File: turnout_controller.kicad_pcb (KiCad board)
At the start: 2 copper layers, 1 part

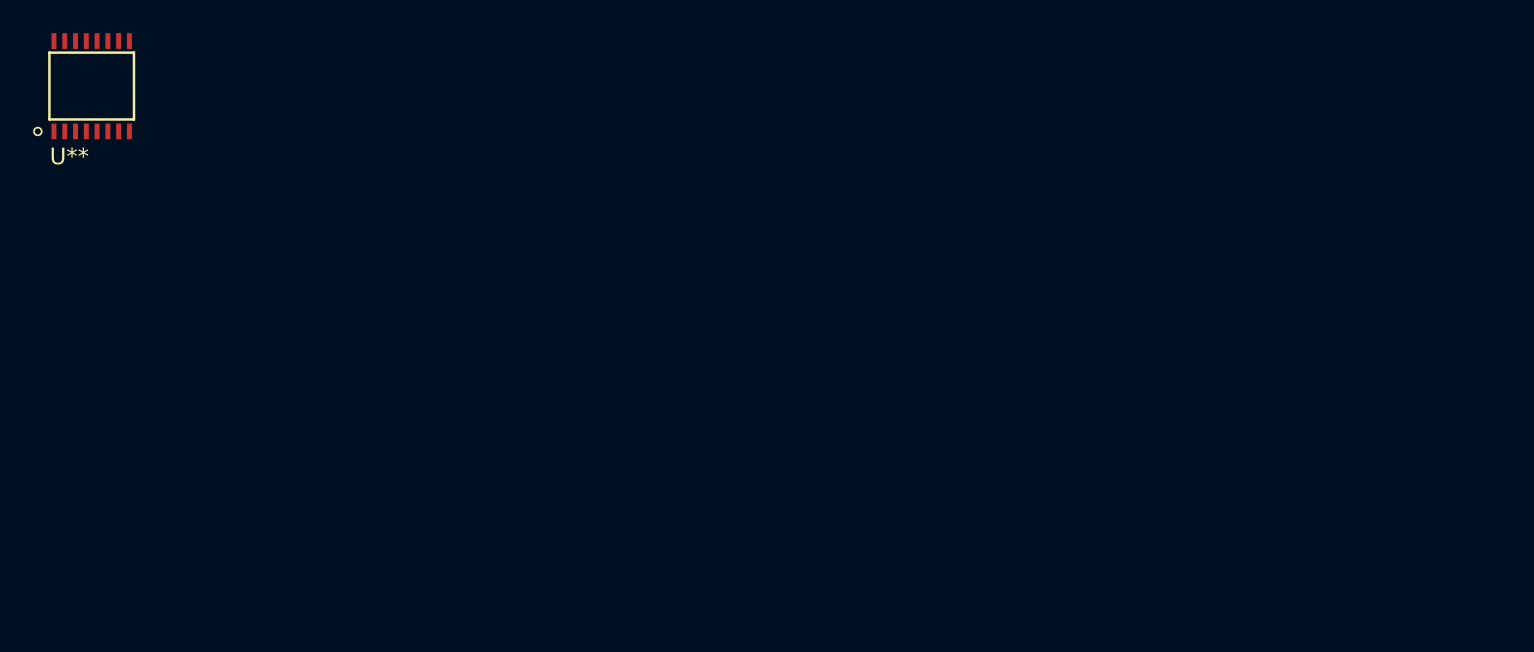
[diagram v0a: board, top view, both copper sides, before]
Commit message: Includes:
New project file
Footprints for buttons, bridge rectifier and edge connectors
initial circuit board layout
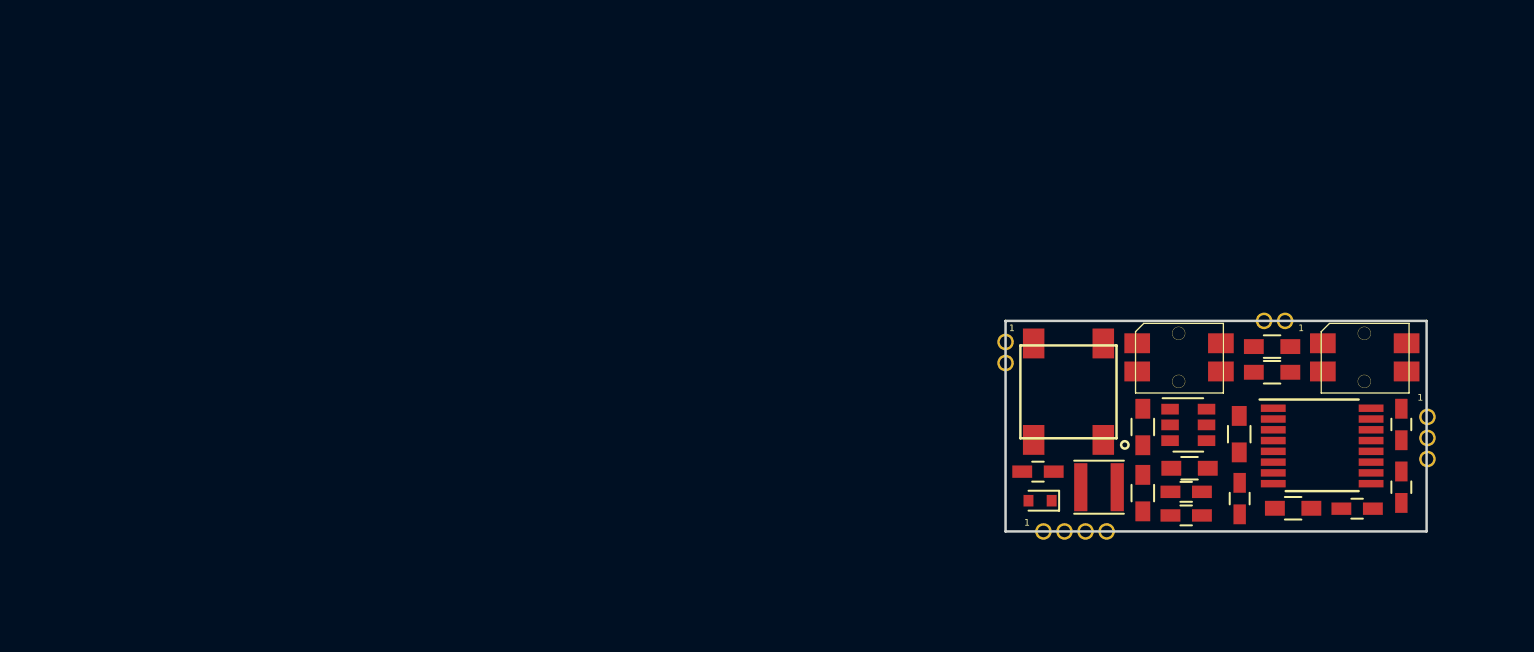
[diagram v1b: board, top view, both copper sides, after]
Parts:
- removed U**: MKE04-TSSOP16, mke04:MKE04-TSSOP16
- added C1: 22u, Capacitors_SMD:C_0603_HandSoldering, F.Cu at (149.6, 82.7)
- added C2: 1u, Capacitors_SMD:C_0603_HandSoldering, F.Cu at (149.6, 84.1)
- added C3: 22u, Capacitors_SMD:C_0603_HandSoldering, F.Cu at (140.6, 81.5)
- added C4: 22u, Capacitors_SMD:C_0603_HandSoldering, F.Cu at (152.8, 83.1)
- added C5: 1u, Capacitors_SMD:C_0603_HandSoldering, F.Cu at (159.9, 83.7)
- added C6: 0.1u, Capacitors_SMD:C_0603_HandSoldering, F.Cu at (162.6, 82.4)
- added C7: 22u, Capacitors_SMD:C_0603_HandSoldering, F.Cu at (162.6, 78.6)
- added D1: D_Schottky, Diodes_SMD:D_SOD-523, F.Cu at (140.8, 83.2)
- added D2: CZ4GP208-HF, Z4GP208-HF:Z4GP208-HF-SMD, F.Cu at (140.0, 75.9)
- added J1: DCC Input, half-connectors:Socket_Strip_Straight_1x02_Pitch1.27mm_at_edge, F.Cu at (138.7, 73.7)
- added J2: Conn_01x04, half-connectors:Socket_Strip_Straight_1x04_Pitch1.27mm_at_edge, F.Cu at (141.0, 85.1)
- added J3: Servo Motor, half-connectors:Socket_Strip_Straight_1x03_Pitch1.27mm_at_edge, F.Cu at (164.1, 78.2)
- added J4: LED Connect, half-connectors:Socket_Strip_Straight_1x02_Pitch1.27mm_at_edge, F.Cu at (155.5, 72.4)
- added L1: 4.7u, Inductors_SMD:L_Taiyo-Yuden_NR-30xx, F.Cu at (144.3, 82.4)
- added R1: 100K, Resistors_SMD:R_0603_HandSoldering, F.Cu at (149.8, 81.3)
- added R2: 10K, Resistors_SMD:R_0603_HandSoldering, F.Cu at (147.0, 82.8)
- added R3: 4.7K, Resistors_SMD:R_0603_HandSoldering, F.Cu at (147.0, 78.8)
- added R4: 59K, Resistors_SMD:R_0603_HandSoldering, F.Cu at (154.8, 75.5)
- added R5: 7.68K, Resistors_SMD:R_0603_HandSoldering, F.Cu at (156.0, 83.7)
- added R6: 40.2K, Resistors_SMD:R_0603_HandSoldering, F.Cu at (152.8, 79.2)
- added R7: 400, Resistors_SMD:R_0603_HandSoldering, F.Cu at (154.8, 73.9)
- added SW1: SW_Push, tt_buttons:HTB1-Button, F.Cu at (162.0, 72.3)
- added SW2: SW_Push, tt_buttons:HTB1-Button, F.Cu at (150.8, 72.3)
- added U1: AP65111A, TO_SOT_Packages_SMD:SOT-23-6, F.Cu at (149.7, 78.7)
- added U2: MKE04P24M48SF0, Housings_SSOP:TSSOP-16_4.4x5mm_Pitch0.65mm, F.Cu at (157.8, 79.9)
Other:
- board outline added: 25.4 x 12.7 mm
- board text added: "1"

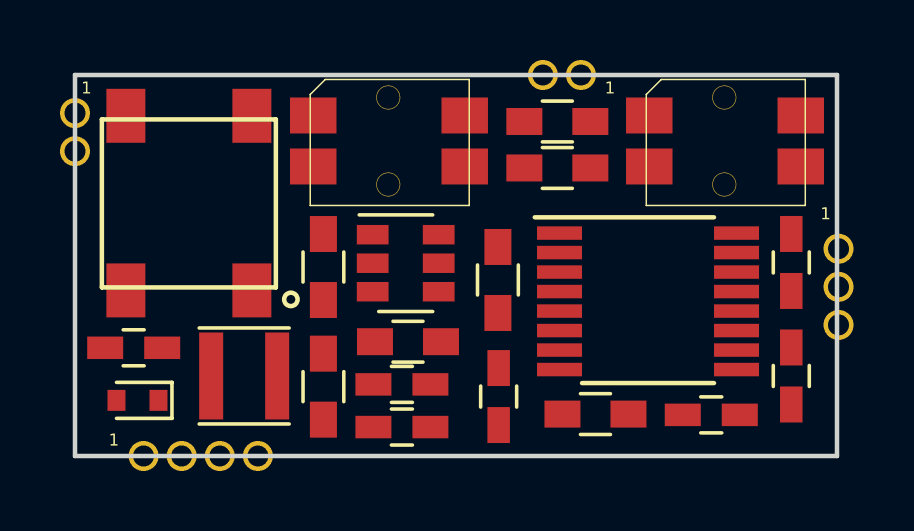
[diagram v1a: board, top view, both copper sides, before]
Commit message: 1. New PCB layout based around new positioning of buttons.
2. Optimizing distance between buck circuit components.

3. Added optional on-board LEDs.
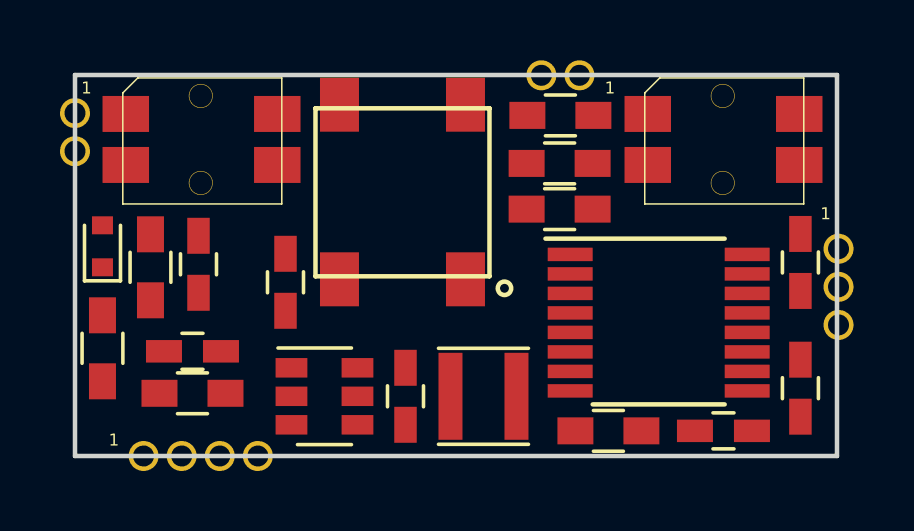
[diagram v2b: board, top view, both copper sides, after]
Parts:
- added D3: LED, LEDs:LED_0603, B.Cu at (157.9, 74.5)
- added D4: LED, LEDs:LED_0603, B.Cu at (140.5, 74.5)
- moved C4 8.06 mm to (145.7, 79.3), turned to 270 degrees
- moved L1 8.01 mm to (152.3, 83.1)
- moved R2 7.47 mm to (139.6, 81.5)
- moved R1 7.39 mm to (142.6, 83.0), turned to 180 degrees
- moved D2 7.13 mm to (147.1, 75.5)
- moved C1 7.07 mm to (142.6, 81.6), turned to 0 degrees
- moved SW2 6.25 mm to (144.6, 72.3)
- moved R3 5.76 mm to (141.2, 78.8)
- moved D1 5.27 mm to (139.6, 78.1), turned to 90 degrees
- moved U1 5.20 mm to (147.0, 83.1)
- moved C3 3.52 mm to (142.8, 78.7), turned to 270 degrees
- moved R6 3.13 mm to (154.8, 76.9), turned to 0 degrees
- moved C2 1.03 mm to (149.7, 83.1), turned to 90 degrees
- moved U2 0.80 mm to (158.1, 80.6)
- moved R5 0.71 mm to (156.5, 84.3)
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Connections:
- net Net-(J4-Pad1) renamed /LED1
- net Net-(J4-Pad2) renamed /LED2
- SW1 pad 1: GND -> Net-(SW1-Pad1)
- SW2 pad 1: GND -> Net-(SW1-Pad1)

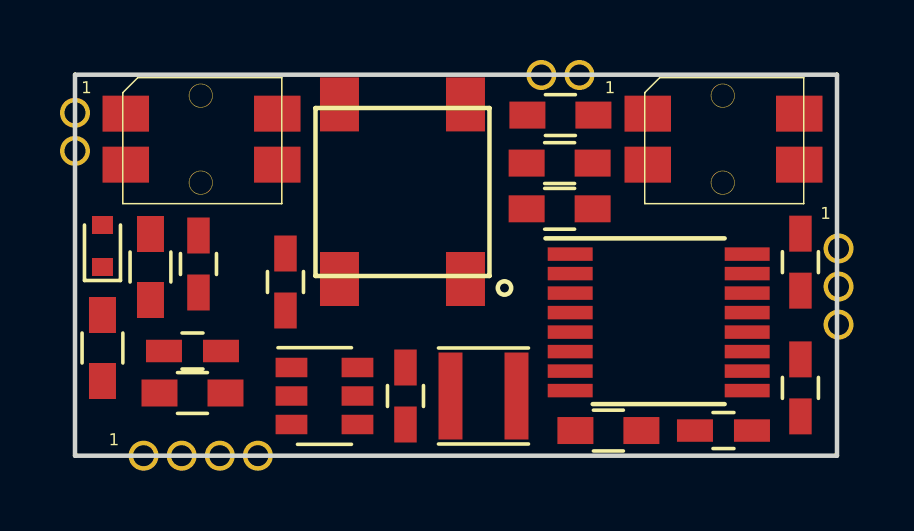
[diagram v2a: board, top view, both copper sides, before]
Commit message: updated PCB layout
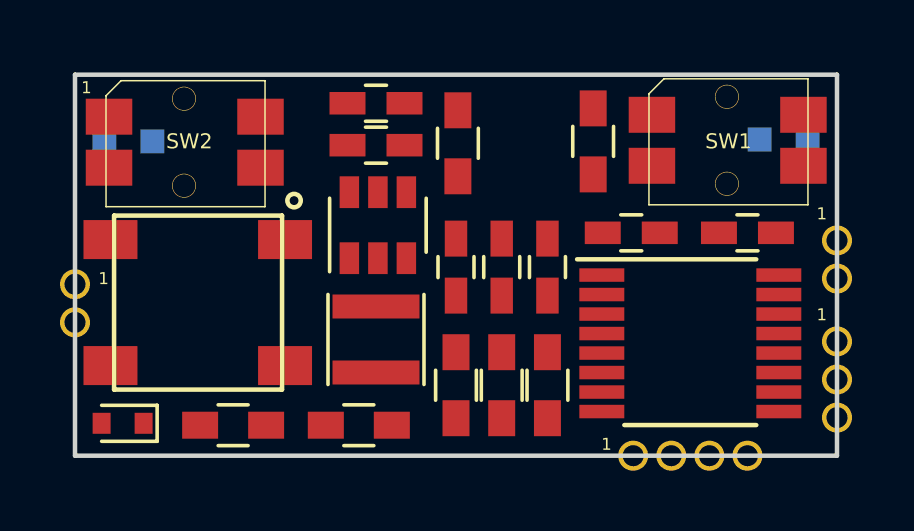
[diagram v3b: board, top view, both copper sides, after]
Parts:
- moved J2 16.3 mm to (157.3, 85.1)
- moved R1 12.1 mm to (151.4, 74.7), turned to 270 degrees
- moved C1 10.3 mm to (148.7, 73.3), turned to 180 degrees
- moved J4 10.2 mm to (164.1, 77.9), turned to 0 degrees
- moved C6 9.34 mm to (154.4, 78.8), turned to 270 degrees
- moved R3 8.72 mm to (148.1, 84.1), turned to 0 degrees
- moved D2 8.66 mm to (142.0, 82.5), turned to 270 degrees
- moved R4 8.17 mm to (151.4, 82.7), turned to 90 degrees
- moved C5 7.27 mm to (157.2, 77.7), turned to 0 degrees
- moved C4 7.23 mm to (152.9, 78.8)
- moved C3 7.12 mm to (148.7, 74.7), turned to 0 degrees
- moved U1 5.97 mm to (148.8, 77.4), turned to 90 degrees
- moved D1 5.95 mm to (140.3, 84.0), turned to 180 degrees
- moved R6 5.89 mm to (154.4, 82.7), turned to 90 degrees
- moved J1 5.72 mm to (138.7, 79.4)
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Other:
- board text added: "SW1"
- board text added: "SW2"

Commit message: Updated PCB layout. Re-arrange buck, and added mounting hole
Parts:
- added REF**: MountingHole_2.2mm_M2, Mounting_Holes:MountingHole_2.2mm_M2, F.Cu at (151.7, 78.6)
- moved C3 7.68 mm to (148.7, 82.4)
- moved C1 7.56 mm to (148.7, 80.9)
- moved R1 4.96 mm to (146.5, 74.5)
- moved C2 4.74 mm to (153.0, 74.4)
- moved C4 4.62 mm to (151.6, 74.4)
- moved U1 2.94 mm to (149.1, 74.5)
- moved L1 2.92 mm to (148.7, 78.3)
- moved C6 0.09 mm to (154.5, 78.9)
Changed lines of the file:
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@@
 (kicad_pcb (version 4) (host pcbnew 4.0.7)
   (general
-    (links 54)
+    (links 0)
     (no_connects 54)
     (area 138.608999 72.314999 164.159001 85.165001)
     (thickness 1.6)
-    (drawings 11)
+    (drawings 10)
     (tracks 0)
     (zones 0)
-    (modules 27)
+    (modules 28)
     (nets 28)
   )
@@
     (mod_text_size 1 1)
     (mod_text_width 0.15)
-    (pad_size 1 1)
-    (pad_drill 0.7)
+    (pad_size 1.7 1.7)
+    (pad_drill 1)
     (pad_to_mask_clearance 0.2)
     (aux_axis_origin 0 0)
@@
   )
   (module Capacitors_SMD:C_0603_HandSoldering (layer F.Cu)
-    (at 148.717 73.3425 180)
+    (at 148.717 80.899 180)
     (descr "Capacitor SMD 0603, hand soldering")
     (tags "capacitor 0603")
@@
   )
   (module Capacitors_SMD:C_0603_HandSoldering (layer F.Cu)
-    (at 151.384 78.8035 270)
+    (at 153.035 74.3585 270)
     (descr "Capacitor SMD 0603, hand soldering")
     (tags "capacitor 0603")
@@
   )
   (module Capacitors_SMD:C_0603_HandSoldering (layer F.Cu)
-    (at 148.717 74.7395)
+    (at 148.717 82.423)
     (descr "Capacitor SMD 0603, hand soldering")
     (tags "capacitor 0603")
@@
   )
   (module Capacitors_SMD:C_0603_HandSoldering (layer F.Cu)
-    (at 152.908 78.8035 270)
+    (at 151.638 74.3585 270)
     (descr "Capacitor SMD 0603, hand soldering")
     (tags "capacitor 0603")
@@
   )
   (module Capacitors_SMD:C_0603_HandSoldering (layer F.Cu)
-    (at 154.432 78.8035 270)
+    (at 154.4955 78.867 270)
     (descr "Capacitor SMD 0603, hand soldering")
     (tags "capacitor 0603")
@@
   )
   (module Inductors_SMD:L_Taiyo-Yuden_NR-30xx (layer F.Cu)
-    (at 148.717 81.2165 270)
+    (at 148.717 78.2955 270)
     (descr "Inductor, Taiyo Yuden, NR series, Taiyo-Yuden_NR-30xx, 3.0mmx3.0mm")
     (tags "inductor taiyo-yuden nr smd")
@@
   )
   (module Resistors_SMD:R_0603_HandSoldering (layer F.Cu)
-    (at 151.4475 74.676 270)
+    (at 146.4945 74.4855 270)
     (descr "Resistor SMD 0603, hand soldering")
     (tags "resistor 0603")
@@
   )
   (module TO_SOT_Packages_SMD:SOT-23-6 (layer F.Cu)
-    (at 148.7805 77.4065 90)
+    (at 149.098 74.4855 90)
     (descr "6-pin SOT-23 package")
     (tags SOT-23-6)
@@
     )
   )
+  (module Mounting_Holes:MountingHole_2.2mm_M2 (layer F.Cu)
+    (at 151.7015 78.613)
+    (descr "Mounting Hole 2.2mm, no annular, M2")
+    (tags "mounting hole 2.2mm no annular m2")
+    (attr virtual)
+    (fp_text reference REF** (at 0 -3.2) (layer F.SilkS) hide
+      (effects (font (size 1 1) (thickness 0.15)))
+    )
+    (fp_text value MountingHole_2.2mm_M2 (at 0 3.2) (layer F.Fab)
+      (effects (font (size 1 1) (thickness 0.15)))
+    )
+    (fp_text user %R (at 0.3 0) (layer F.Fab) hide
+      (effects (font (size 1 1) (thickness 0.15)))
+    )
+    (fp_circle (center 0 0) (end 2.2 0) (layer Cmts.User) (width 0.15))
+    (fp_circle (center 0 0) (end 2.45 0) (layer F.CrtYd) (width 0.05))
+    (pad "" thru_hole circle (at 0 0) (size 1.7 1.7) (drill 1) (layers *.Cu *.Mask))
+  )
   (gr_text SW1 (at 160.4645 74.6125) (layer F.SilkS)
     (effects (font (size 0.5 0.5) (thickness 0.125)))
@@
     (effects (font (size 0.4 0.4) (thickness 0.075)))
   )
-  (gr_text 1 (at 139.065 72.8218) (layer F.SilkS)
-    (effects (font (size 0.4 0.4) (thickness 0.075)))
-  )

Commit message: Connector improvements. Initial trace layout.
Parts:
- removed REF**: MountingHole_2.2mm_M2, Mounting_Holes:MountingHole_2.2mm_M2
- added J5: MOT_POWER, half-connectors:Socket_Strip_Straight_1x01_Pitch1.27mm_at_edge, F.Cu at (164.1, 82.3)
- added J6: MOT_GND, half-connectors:Socket_Strip_Straight_1x01_Pitch1.27mm_at_edge, F.Cu at (164.1, 83.9)
- added J7: LED_1, half-connectors:Socket_Strip_Straight_1x01_Pitch1.27mm_at_edge, F.Cu at (164.1, 77.0)
- added J8: LED_2, half-connectors:Socket_Strip_Straight_1x01_Pitch1.27mm_at_edge, F.Cu at (164.1, 78.6)
- J1: value DCC Input -> DCC_A; footprint half-connectors:Socket_Strip_Straight_1x02_Pitch1.27mm_at_edge -> half-connectors:Socket_Strip_Straight_1x01_Pitch1.27mm_at_edge
- J2: value Conn_01x04 -> DCC_B; footprint half-connectors:Socket_Strip_Straight_1x04_Pitch1.27mm_at_edge -> half-connectors:Socket_Strip_Straight_1x01_Pitch1.27mm_at_edge
- J3: value Servo Motor -> PROG; footprint half-connectors:Socket_Strip_Straight_1x03_Pitch1.27mm_at_edge -> half-connectors:Socket_Strip_Straight_1x04_Pitch1.27mm_at_edge
- J4: value LED Connect -> MOT_CNTL; footprint half-connectors:Socket_Strip_Straight_1x02_Pitch1.27mm_at_edge -> half-connectors:Socket_Strip_Straight_1x01_Pitch1.27mm_at_edge
- moved J2 19.3 mm to (138.7, 80.0), turned to 0 degrees
- moved J3 7.68 mm to (157.4, 85.1), turned to 90 degrees
- moved J1 4.83 mm to (138.7, 84.2)
- moved J4 2.73 mm to (164.1, 80.6)
- moved D1 0.85 mm to (141.1, 84.2)
- moved R2 0.52 mm to (144.5, 84.2)
- moved R3 0.40 mm to (148.5, 84.2)
- moved C3 0.19 mm to (148.7, 82.2)
- moved C1 0.06 mm to (148.7, 80.8)
- turned C7 to 0 degrees
- turned R7 to 90 degrees
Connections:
- D3 pad 1: /LED2 -> /LED1
- D3 pad 2: /LED1 -> /LED2
- D4 pad 1: /LED1 -> /LED2
- D4 pad 2: /LED2 -> /LED1
- J1 pad 1: /DCC_B -> /DCC_A
- J2 pad 1: GND -> /DCC_B
- J3 pad 1: Net-(J3-Pad1) -> GND
- J3 pad 2: 5V -> /SWD_IO
- J3 pad 3: GND -> /KEY_UP
- J4 pad 1: /LED1 -> Net-(J4-Pad1)
- SW1 pad 1: Net-(SW1-Pad1) -> GND
- SW2 pad 1: Net-(SW1-Pad1) -> GND
- U2 pad 7: Net-(J3-Pad1) -> Net-(J4-Pad1)
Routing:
- net 5V: track 0.00 -> 30.6 mm, vias 0 -> 1
- net /DCC_IN: track 0.00 -> 19.5 mm, vias 0 -> 2
- net /KEY_UP: track 0.00 -> 14.1 mm, vias 0 -> 2
- net 12V: track 0.00 -> 9.39 mm
- net /DCC_A: track 0.00 -> 7.83 mm
- net /SWD_IO: track 0.00 -> 7.20 mm
- net Net-(C2-Pad2): track 0.00 -> 6.93 mm
- net /LED1: track 0.00 -> 3.00 mm
- net /DCC_B: track 0.00 -> 2.72 mm
- net Net-(D1-Pad1): track 0.00 -> 1.57 mm
- net Net-(R4-Pad2): track 0.00 -> 1.52 mm

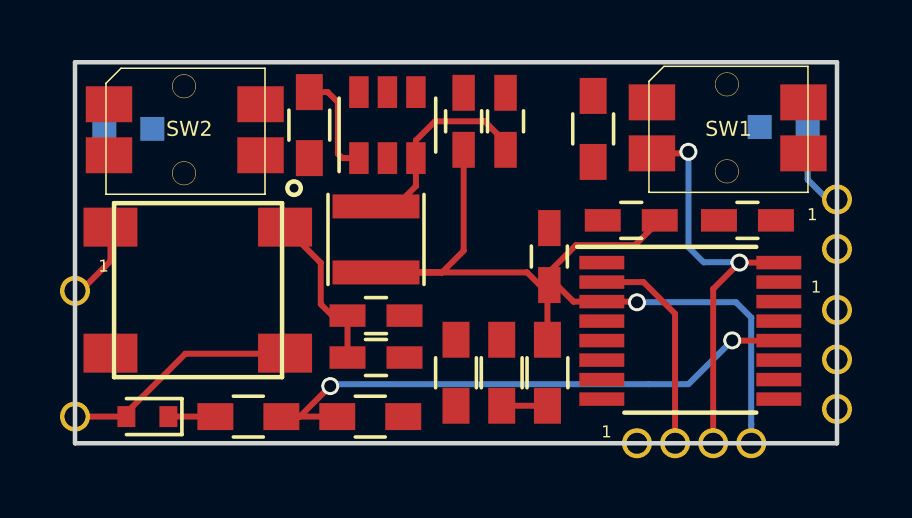
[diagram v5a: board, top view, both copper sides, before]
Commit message: First layout. Connections routed. Ground fill remains.
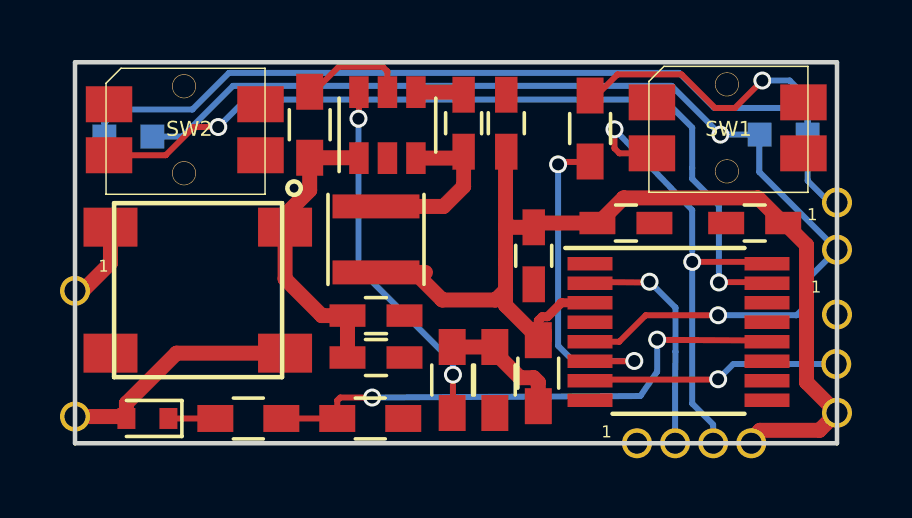
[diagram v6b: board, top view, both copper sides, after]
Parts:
- moved J6 3.15 mm to (164.1, 80.8)
- moved J4 1.80 mm to (164.1, 82.4)
- moved J5 1.78 mm to (164.1, 84.1)
- moved C4 1.42 mm to (153.1, 74.4)
- moved C2 1.40 mm to (151.6, 74.4)
- moved C6 0.52 mm to (154.0, 78.8), turned to 90 degrees
- moved U2 0.40 mm to (158.8, 81.4)
- moved R5 0.33 mm to (152.7, 83.0), turned to 270 degrees
- moved R6 0.31 mm to (154.1, 82.8)
- moved R4 0.27 mm to (151.3, 83.0)
- moved C7 0.26 mm to (161.3, 77.7), turned to 180 degrees
- moved D4 0.25 mm to (140.5, 74.9)
- moved D3 0.25 mm to (162.3, 74.8)
- moved C5 0.20 mm to (157.0, 77.7), turned to 180 degrees
- moved R7 0.10 mm to (155.9, 74.6)
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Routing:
- net /LED2: track 0.00 -> 36.5 mm, vias 0 -> 2
- net /LED1: track 3.00 -> 38.4 mm, vias 0 -> 1
- net /KEY_DN: track 0.00 -> 28.2 mm, vias 0 -> 2
- net Net-(R4-Pad1): track 0.00 -> 12.4 mm, vias 0 -> 2
- net Net-(R7-Pad1): track 0.00 -> 11.5 mm, vias 0 -> 2
- net Net-(J4-Pad1): track 0.00 -> 8.03 mm, vias 0 -> 1
- net 5V: track 30.6 -> 37.9 mm, vias 1 -> 0
- net /KEY_UP: track 14.1 -> 17.9 mm
- net Net-(R1-Pad2): track 0.00 -> 3.69 mm
- net Net-(R4-Pad2): track 1.52 -> 4.48 mm
- net Net-(C2-Pad1): track 0.00 -> 1.50 mm
- net Net-(C2-Pad2): track 6.93 -> 6.03 mm
- net /DCC_IN: track 19.5 -> 18.7 mm
- net 12V: track 9.39 -> 10.0 mm
- net /SWD_IO: track 7.20 -> 7.34 mm, vias 0 -> 1
